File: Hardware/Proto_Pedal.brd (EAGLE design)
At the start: 85.1 x 110.5 mm, 124 parts, among them Q1 2.5A/30V

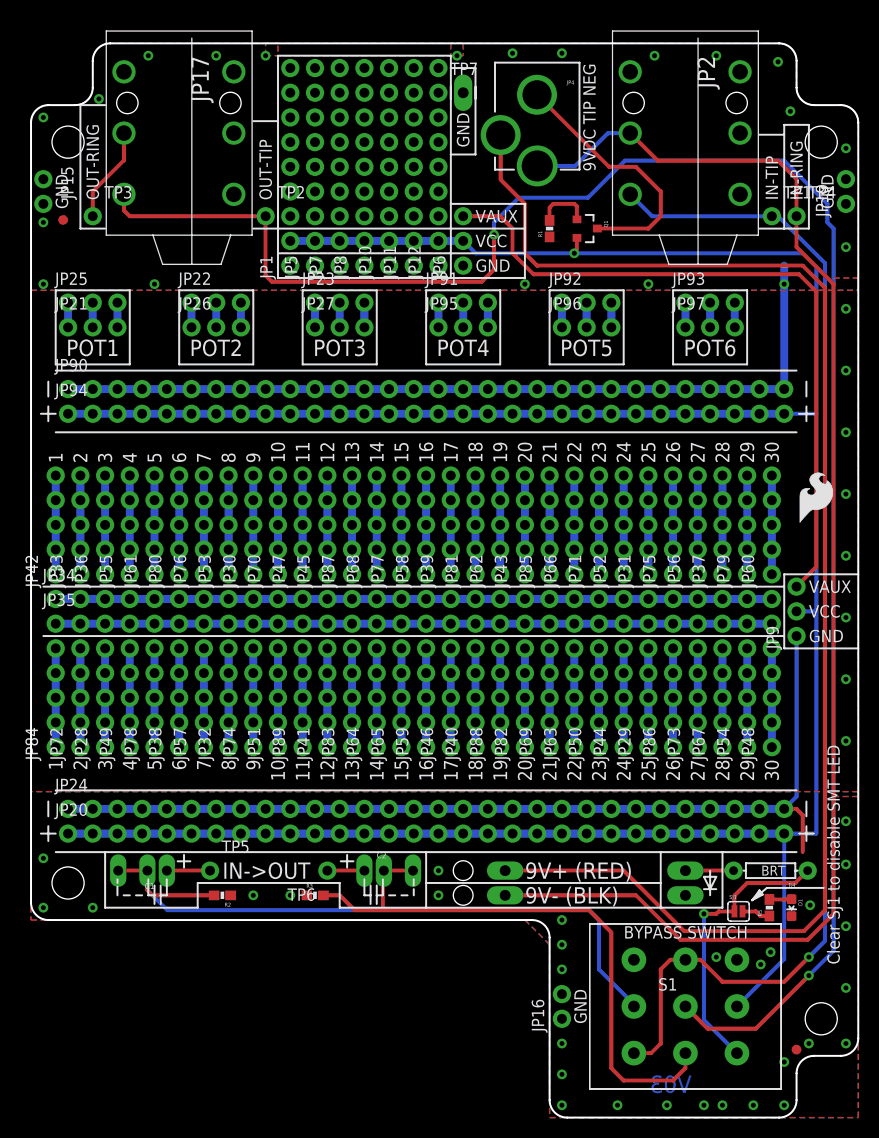
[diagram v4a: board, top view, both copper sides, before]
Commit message: Silkscreen touchups from V03 proto.
Prepping for redboard review.
Rolling version to V10.
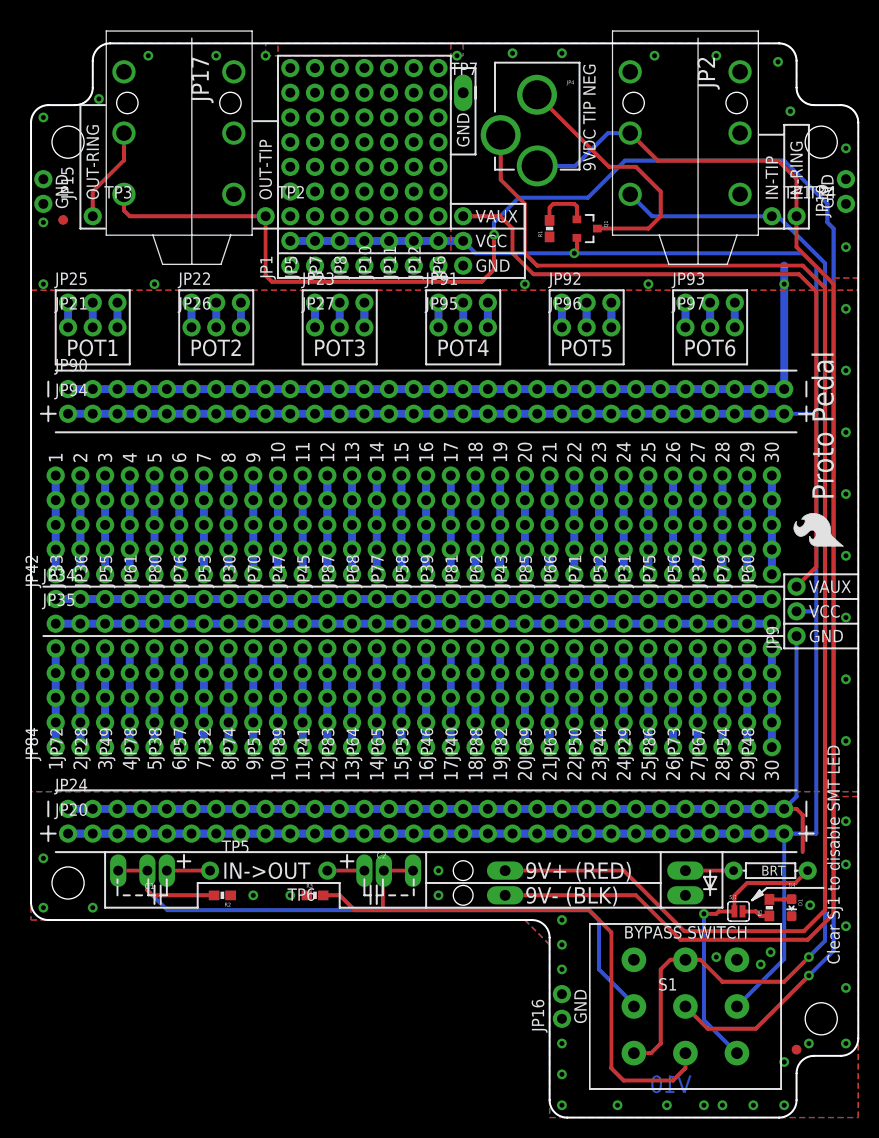
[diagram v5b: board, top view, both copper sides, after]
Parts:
- moved LOGO3 5.68 mm to (83.8, 58.4), turned to 90 degrees
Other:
- board text added: "BRT"
- board text added: "V10"
- board text removed: "V03"
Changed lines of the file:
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@@
 <?xml version="1.0" encoding="utf-8"?>
 <!DOCTYPE eagle SYSTEM "eagle.dtd">
-<eagle version="7.3.0">
+<eagle version="7.5.0">
 <drawing>
 <settings>
@@
 <setting verticaltext="up"/>
 </settings>
-<grid distance="0.1" unitdist="inch" unit="inch" style="lines" multiple="1" display="yes" altdistance="0.01" altunitdist="inch" altunit="inch"/>
+<grid distance="0.05" unitdist="inch" unit="inch" style="lines" multiple="1" display="yes" altdistance="0.005" altunitdist="inch" altunit="inch"/>
 <layers>
 <layer number="1" name="Top" color="4" fill="1" visible="yes" active="yes"/>
@@
 <layer number="27" name="tValues" color="7" fill="1" visible="no" active="yes"/>
 <layer number="28" name="bValues" color="7" fill="1" visible="no" active="yes"/>
-<layer number="29" name="tStop" color="7" fill="3" visible="yes" active="yes"/>
-<layer number="30" name="bStop" color="7" fill="6" visible="yes" active="yes"/>
+<layer number="29" name="tStop" color="7" fill="3" visible="no" active="yes"/>
+<layer number="30" name="bStop" color="7" fill="6" visible="no" active="yes"/>
 <layer number="31" name="tCream" color="7" fill="4" visible="no" active="yes"/>
 <layer number="32" name="bCream" color="7" fill="5" visible="no" active="yes"/>
@@
 <text x="45.72" y="92.71" size="1.27" layer="21" font="vector" ratio="15" align="center-left">VAUX</text>
 <text x="45.72" y="90.17" size="1.27" layer="21" font="vector" ratio="15" align="center-left">VCC</text>
-<wire x1="77.47" y1="48.26" x2="77.47" y2="55.88" width="0.2032" layer="21"/>
+<wire x1="77.47" y1="48.26" x2="77.47" y2="50.8" width="0.2032" layer="21"/>
+<wire x1="77.47" y1="50.8" x2="77.47" y2="53.34" width="0.2032" layer="21"/>
+<wire x1="77.47" y1="53.34" x2="77.47" y2="55.88" width="0.2032" layer="21"/>
 <wire x1="85.09" y1="55.88" x2="77.47" y2="55.88" width="0.2032" layer="21"/>
 <wire x1="85.09" y1="48.26" x2="77.47" y2="48.26" width="0.2032" layer="21"/>
@@
 <wire x1="77.47" y1="55.88" x2="85.09" y2="55.88" width="0.2032" layer="22"/>
 <wire x1="77.47" y1="48.26" x2="77.47" y2="49.53" width="0.2032" layer="22"/>
-<wire x1="77.47" y1="49.53" x2="77.47" y2="54.61" width="0.2032" layer="22"/>
+<wire x1="77.47" y1="49.53" x2="77.47" y2="50.8" width="0.2032" layer="22"/>
+<wire x1="77.47" y1="50.8" x2="77.47" y2="53.34" width="0.2032" layer="22"/>
+<wire x1="77.47" y1="53.34" x2="77.47" y2="54.61" width="0.2032" layer="22"/>
 <wire x1="77.47" y1="54.61" x2="77.47" y2="55.88" width="0.2032" layer="22"/>
 <wire x1="77.47" y1="48.26" x2="85.09" y2="48.26" width="0.2032" layer="22"/>
@@
 <wire x1="64.77" y1="27.305" x2="64.77" y2="24.13" width="0.2032" layer="22"/>
 <wire x1="40.64" y1="24.13" x2="40.64" y2="21.59" width="0.2032" layer="22"/>
-<wire x1="50.8" y1="86.36" x2="43.18" y2="86.36" width="0.2032" layer="22"/>
 <wire x1="50.8" y1="93.98" x2="43.18" y2="93.98" width="0.2032" layer="22"/>
 <wire x1="43.18" y1="93.98" x2="43.18" y2="91.44" width="0.2032" layer="22"/>
-<wire x1="50.8" y1="93.98" x2="50.8" y2="86.36" width="0.2032" layer="22"/>
+<wire x1="50.8" y1="93.98" x2="50.8" y2="91.44" width="0.2032" layer="22"/>
 <text x="54.61" y="101.6" size="1.27" layer="22" font="vector" ratio="15" rot="SMR270" align="top-center">9VDC IN
 TIP NEG</text>
 <circle x="52.07" y="108.839" radius="0.381" width="0" layer="22"/>
+<wire x1="50.8" y1="91.44" x2="50.8" y2="88.9" width="0.2032" layer="22"/>
+<wire x1="50.8" y1="88.9" x2="50.8" y2="86.36" width="0.2032" layer="22"/>
 <wire x1="50.8" y1="108.839" x2="52.07" y2="107.569" width="0.254" layer="22" curve="90"/>
 <wire x1="52.07" y1="107.569" x2="52.959" y2="107.95" width="0.254" layer="22" curve="45"/>
@@
 <text x="22.86" y="87.63" size="2.1844" layer="22" font="vector" ratio="15" rot="MR0">Proto Pedal</text>
 <text x="82.55" y="15.748" size="1.27" layer="21" font="vector" ratio="15" rot="R90" align="center-left">Clear SJ1 to disable SMT LED</text>
-<wire x1="43.18" y1="86.36" x2="50.8" y2="86.36" width="0.2032" layer="21"/>
 <wire x1="43.18" y1="93.98" x2="50.8" y2="93.98" width="0.2032" layer="21"/>
-<wire x1="43.18" y1="93.98" x2="43.18" y2="86.36" width="0.2032" layer="21"/>
 <wire x1="50.8" y1="93.98" x2="50.8" y2="91.44" width="0.2032" layer="21"/>
 <wire x1="50.8" y1="91.44" x2="50.8" y2="88.9" width="0.2032" layer="21"/>
@@
 <wire x1="50.8" y1="88.9" x2="25.4" y2="88.9" width="0.2032" layer="21"/>
 <wire x1="25.4" y1="88.9" x2="25.4" y2="86.36" width="0.2032" layer="21"/>
-<wire x1="25.4" y1="86.36" x2="43.18" y2="86.36" width="0.2032" layer="21"/>
+<wire x1="25.4" y1="86.36" x2="50.8" y2="86.36" width="0.2032" layer="21"/>
 <wire x1="25.4" y1="88.9" x2="25.4" y2="91.44" width="0.2032" layer="21"/>
-<wire x1="25.4" y1="91.44" x2="50.8" y2="91.44" width="0.2032" layer="21"/>
+<wire x1="25.4" y1="91.44" x2="43.18" y2="91.44" width="0.2032" layer="21"/>
+<wire x1="43.18" y1="91.44" x2="50.8" y2="91.44" width="0.2032" layer="21"/>
 <wire x1="25.4" y1="102.489" x2="25.4" y2="109.22" width="0.2032" layer="21"/>
 <wire x1="25.4" y1="109.22" x2="43.18" y2="109.22" width="0.2032" layer="21"/>
@@
 <wire x1="43.18" y1="107.95" x2="43.18" y2="109.22" width="0.2032" layer="22"/>
 <wire x1="43.18" y1="91.44" x2="25.4" y2="91.44" width="0.2032" layer="22"/>
-<wire x1="43.18" y1="86.36" x2="25.4" y2="86.36" width="0.2032" layer="22"/>
-<wire x1="43.18" y1="91.44" x2="43.18" y2="88.9" width="0.2032" layer="22"/>
-<wire x1="43.18" y1="88.9" x2="43.18" y2="86.36" width="0.2032" layer="22"/>
+<wire x1="50.8" y1="86.36" x2="25.4" y2="86.36" width="0.2032" layer="22"/>
 <wire x1="25.4" y1="91.44" x2="25.4" y2="88.9" width="0.2032" layer="22"/>
 <wire x1="25.4" y1="88.9" x2="25.4" y2="86.36" width="0.2032" layer="22"/>
-<wire x1="43.18" y1="88.9" x2="25.4" y2="88.9" width="0.2032" layer="22"/>
+<wire x1="50.8" y1="88.9" x2="25.4" y2="88.9" width="0.2032" layer="22"/>
 <text x="24.13" y="94.361" size="1.27" layer="22" font="vector" ratio="15" rot="MR90" align="center-left">OUT-TIP</text>
 <text x="76.2" y="94.361" size="1.27" layer="22" font="vector" ratio="15" rot="MR90" align="center-left">IN-TIP</text>
@@
 <wire x1="32.512" y1="27.016" x2="32.512" y2="25.708" width="0.2032" layer="22"/>
 <text x="19.177" y="25.4" size="1.6764" layer="22" font="vector" ratio="15" rot="MR180" align="center-left">OUT&lt;-IN</text>
-<text x="67.945" y="2.54" size="1.778" layer="16" font="vector" ratio="15" rot="MR0">V03</text>
+<text x="67.945" y="2.54" size="1.778" layer="16" font="vector" ratio="15" rot="MR0">V10</text>
 <dimension x1="0" y1="0" x2="0" y2="110.49" x3="-16.51" y3="55.245" textsize="1.778" textratio="15" layer="47" unit="inch"/>
 <text x="11.43" y="-19.05" size="2.54" layer="47" ratio="15">All Dimensions in inches
@@
 <wire x1="79.756" y1="73.152" x2="79.756" y2="71.628" width="0.2032" layer="22"/>
 <wire x1="80.518" y1="72.39" x2="78.994" y2="72.39" width="0.2032" layer="22"/>
+<wire x1="43.18" y1="93.98" x2="43.18" y2="91.44" width="0.2032" layer="21"/>
+<wire x1="50.8" y1="91.44" x2="43.18" y2="91.44" width="0.2032" layer="22"/>
+<wire x1="7.62" y1="91.44" x2="7.62" y2="104.14" width="0.2032" layer="22"/>
+<wire x1="73.533" y1="26.162" x2="78.613" y2="26.162" width="0.2032" layer="22"/>
+<wire x1="78.613" y1="26.162" x2="78.613" y2="25.4" width="0.2032" layer="22"/>
+<wire x1="78.613" y1="25.4" x2="78.613" y2="24.638" width="0.2032" layer="22"/>
+<wire x1="78.613" y1="24.638" x2="73.533" y2="24.638" width="0.2032" layer="22"/>
+<wire x1="73.533" y1="24.638" x2="73.533" y2="25.4" width="0.2032" layer="22"/>
+<wire x1="73.533" y1="25.4" x2="73.533" y2="26.162" width="0.2032" layer="22"/>
+<wire x1="73.533" y1="25.4" x2="73.279" y2="25.4" width="0.2032" layer="22"/>
+<wire x1="78.867" y1="25.4" x2="78.613" y2="25.4" width="0.2032" layer="22"/>
+<text x="77.343" y="24.892" size="1.016" layer="22" font="vector" ratio="15" rot="MR0">BRT</text>
+<wire x1="85.09" y1="53.34" x2="77.47" y2="53.34" width="0.2032" layer="21"/>
+<wire x1="85.09" y1="50.8" x2="77.47" y2="50.8" width="0.2032" layer="21"/>
+<wire x1="77.47" y1="50.8" x2="85.09" y2="50.8" width="0.2032" layer="22"/>
+<wire x1="77.47" y1="53.34" x2="85.09" y2="53.34" width="0.2032" layer="22"/>
+<text x="82.55" y="63.5" size="2.1844" layer="21" font="vector" ratio="15" rot="R90">Proto Pedal</text>
 </plain>
 <attributes>
@@
 </element>
 <element name="TP7" library="SparkFun-Connectors" package="1X01_LONGPAD" value="Out Ring" x="44.45" y="105.41"/>
-<element name="LOGO3" library="SparkFun-Aesthetics" package="SFE_LOGO_FLAME_.2" value="SFE_LOGO_FLAME.2_INCH" x="78.74" y="60.96"/>
+<element name="LOGO3" library="SparkFun-Aesthetics" package="SFE_LOGO_FLAME_.2" value="SFE_LOGO_FLAME.2_INCH" x="83.82" y="58.42" rot="R90"/>
 </elements>
 <signals>

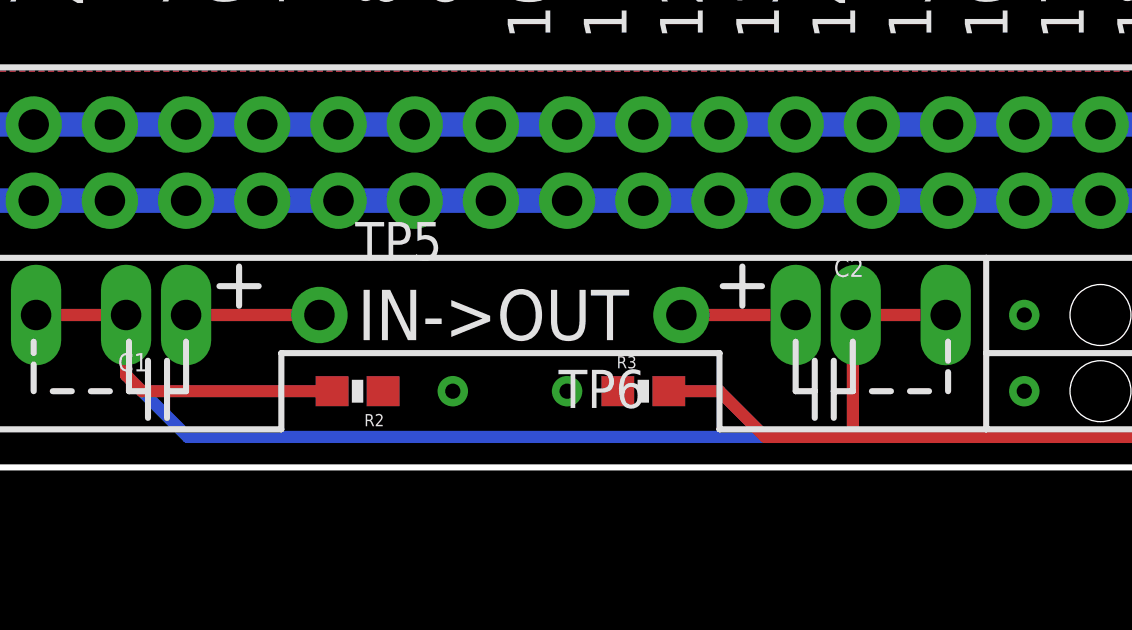
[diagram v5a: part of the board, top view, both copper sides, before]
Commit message: Updates to board following group review.
Added bottom-layer traces on I/O caps.
Updated dimensions for  standoff holes.
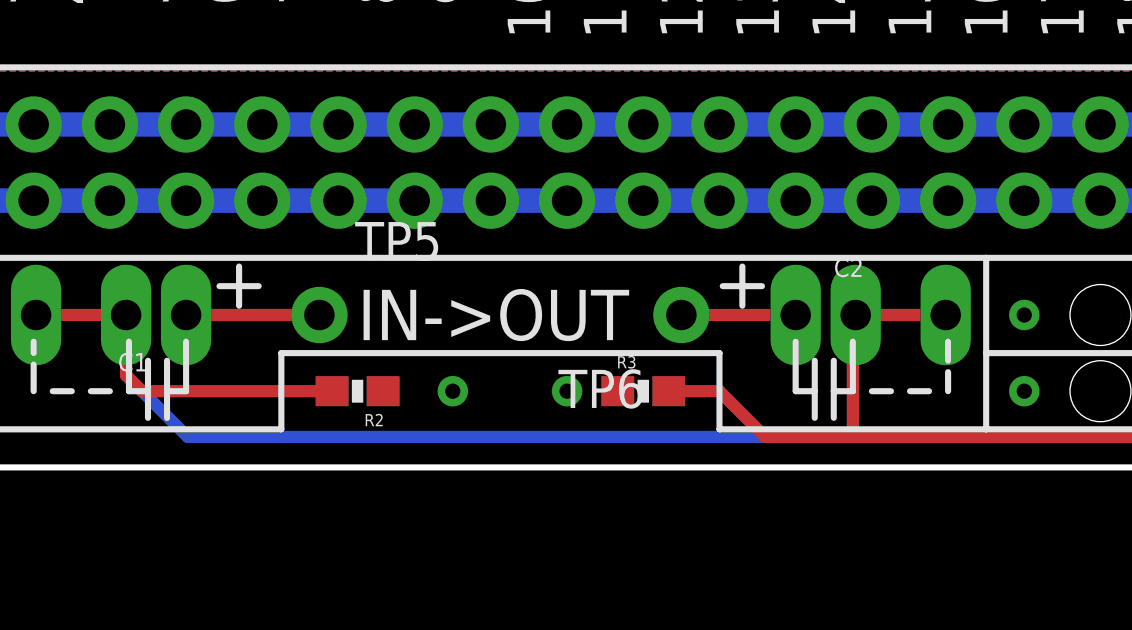
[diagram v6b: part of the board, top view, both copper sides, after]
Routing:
- net N$67: track 4.44 -> 8.89 mm
- net FX_OUT: track 62.5 -> 65.5 mm
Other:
- board text added: "4x Standoff holes clear 4-40 thread."
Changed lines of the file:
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@@
 <layer number="45" name="Holes" color="7" fill="1" visible="yes" active="yes"/>
 <layer number="46" name="Milling" color="3" fill="1" visible="no" active="yes"/>
-<layer number="47" name="Measures" color="7" fill="1" visible="no" active="yes"/>
+<layer number="47" name="Measures" color="7" fill="1" visible="yes" active="yes"/>
 <layer number="48" name="Document" color="7" fill="1" visible="no" active="yes"/>
 <layer number="49" name="Reference" color="7" fill="1" visible="no" active="yes"/>
@@
 <text x="19.177" y="25.4" size="1.6764" layer="22" font="vector" ratio="15" rot="MR180" align="center-left">OUT&lt;-IN</text>
 <text x="67.945" y="2.54" size="1.778" layer="16" font="vector" ratio="15" rot="MR0">V10</text>
-<dimension x1="0" y1="0" x2="0" y2="110.49" x3="-16.51" y3="55.245" textsize="1.778" textratio="15" layer="47" unit="inch"/>
+<dimension x1="0" y1="0" x2="0" y2="110.49" x3="-29.21" y3="55.245" textsize="2.54" textratio="15" layer="47" unit="inch"/>
 <text x="11.43" y="-19.05" size="2.54" layer="47" ratio="15">All Dimensions in inches
 PCB fits inside a 1590BB type case.</text>
-<dimension x1="0" y1="110.49" x2="85.09" y2="110.49" x3="42.545" y3="154.94" textsize="2.54" textratio="15" layer="47" unit="inch"/>
-<dimension x1="0" y1="110.49" x2="68.58" y2="110.49" x3="34.29" y3="146.05" textsize="2.54" textratio="15" layer="47" unit="inch"/>
-<dimension x1="0" y1="110.49" x2="16.51" y2="110.49" x3="8.255" y3="130.81" textsize="2.54" textratio="15" layer="47" unit="inch"/>
+<dimension x1="0" y1="110.49" x2="85.09" y2="110.49" x3="42.545" y3="162.56" textsize="2.54" textratio="15" layer="47" unit="inch"/>
+<dimension x1="0" y1="110.49" x2="68.58" y2="110.49" x3="34.29" y3="154.94" textsize="2.54" textratio="15" layer="47" unit="inch"/>
+<dimension x1="0" y1="110.49" x2="16.51" y2="110.49" x3="8.255" y3="142.24" textsize="2.54" textratio="15" layer="47" unit="inch"/>
 <dimension x1="67.31" y1="24.13" x2="0" y2="0" x3="33.655" y3="-26.67" textsize="2.54" textratio="15" layer="47" dtype="horizontal" unit="inch"/>
 <dimension x1="67.31" y1="11.43" x2="-8.89" y2="0" x3="-6.35" y3="5.715" textsize="2.54" textratio="15" layer="47" dtype="vertical" unit="inch"/>
@@
 <wire x1="15.082" y1="26.362" x2="16.39" y2="26.362" width="0.2032" layer="22"/>
 <wire x1="15.736" y1="27.016" x2="15.736" y2="25.708" width="0.2032" layer="22"/>
-<dimension x1="0" y1="110.49" x2="52.07" y2="110.49" x3="26.035" y3="138.684" textsize="2.54" textratio="15" layer="47" unit="inch"/>
+<dimension x1="0" y1="110.49" x2="52.07" y2="110.49" x3="26.035" y3="148.844" textsize="2.54" textratio="15" layer="47" unit="inch"/>
 <text x="2.54" y="95.25" size="1.27" layer="22" font="vector" ratio="15" rot="MR270" align="top-center">GND</text>
 <text x="2.54" y="95.25" size="1.27" layer="21" font="vector" ratio="15" rot="R90" align="top-center">GND</text>
@@
 <wire x1="77.47" y1="53.34" x2="85.09" y2="53.34" width="0.2032" layer="22"/>
 <text x="82.55" y="63.5" size="2.1844" layer="21" font="vector" ratio="15" rot="R90">Proto Pedal</text>
+<dimension x1="78.74" y1="0" x2="81.28" y2="10.16" x3="109.22" y3="5.08" textsize="2.54" textratio="15" layer="47" dtype="vertical" unit="inch"/>
+<dimension x1="3.81" y1="0" x2="3.81" y2="100.33" x3="-20.2457" y3="50.165" textsize="2.54" textratio="15" layer="47" unit="inch"/>
+<dimension x1="0" y1="101.6" x2="3.81" y2="101.6" x3="1.905" y3="133.35" textsize="2.54" textratio="15" layer="47" unit="inch"/>
+<dimension x1="81.28" y1="10.16" x2="100.33" y2="19.05" x3="107.95" y3="19.05" textsize="2.54" textratio="15" layer="47" dtype="leader" unit="inch"/>
+<text x="101.6" y="20.32" size="2.54" layer="47" ratio="15">4x Standoff holes clear 4-40 thread.</text>
 </plain>
 <attributes>
@@
 <wire x1="36.29" y1="25.4" x2="36.195" y2="25.305" width="0.4064" layer="1"/>
 <wire x1="36.195" y1="25.305" x2="36.195" y2="21.336" width="0.4064" layer="1"/>
+<wire x1="36.275" y1="25.4" x2="39.29" y2="25.4" width="0.4064" layer="16"/>
 </signal>
 <signal name="N$5">
@@
 <contactref element="TP5" pad="1"/>
 <wire x1="13.97" y1="25.4" x2="18.415" y2="25.4" width="0.4064" layer="1"/>
+<wire x1="18.415" y1="25.4" x2="13.97" y2="25.4" width="0.4064" layer="16"/>
 </signal>
 <signal name="N$68">
